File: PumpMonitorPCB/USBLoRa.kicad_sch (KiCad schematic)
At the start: 7 parts, among them J4 USB_C_Receptacle_USB2.0_16P, U7 WIO-SX1262, U8 TPD3E001DRLR

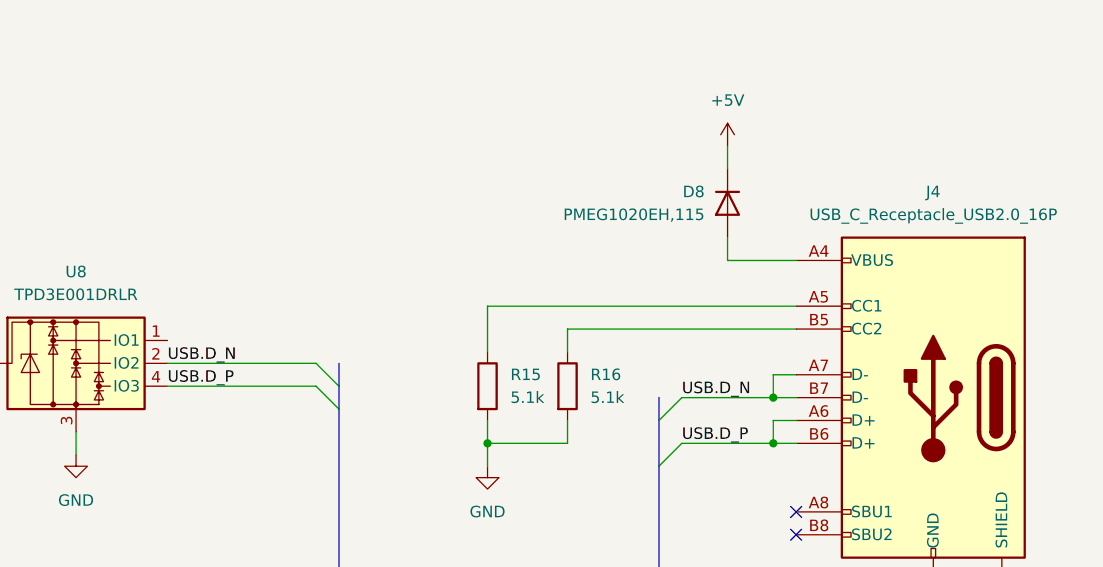
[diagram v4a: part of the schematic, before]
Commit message: Rejigged auxilliary connectors, experimetning with kiclearance.
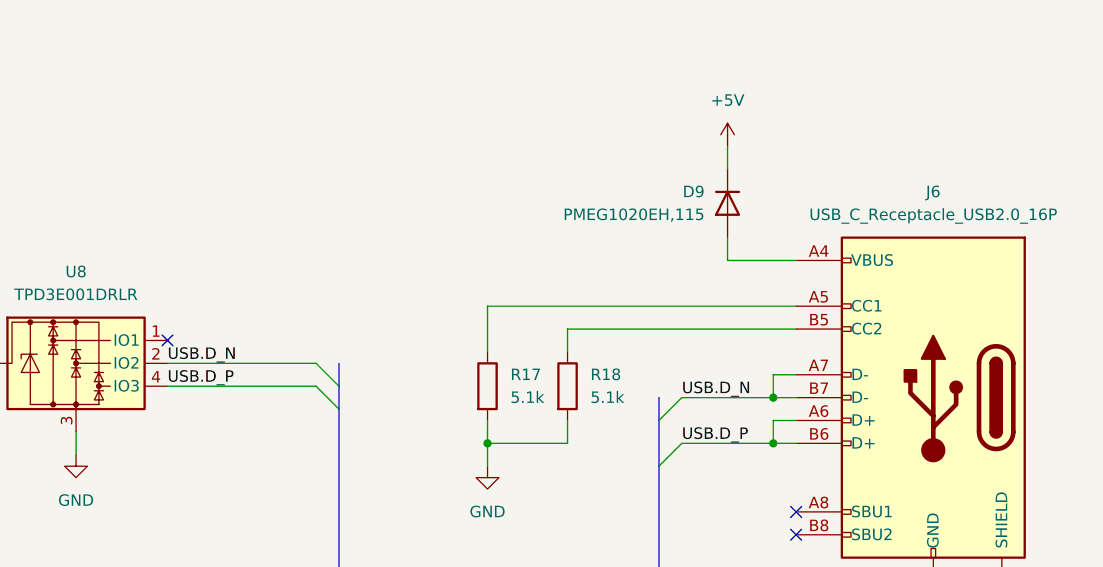
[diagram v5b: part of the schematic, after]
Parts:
- C17: footprint Capacitor_SMD:C_0805_2012Metric_Pad1.18x1.45mm_HandSolder -> Capacitor_SMD:C_0603_1608Metric_Pad1.08x0.95mm_HandSolder
- R17: renamed from R15; footprint Resistor_SMD:R_0805_2012Metric_Pad1.20x1.40mm_HandSolder -> Resistor_SMD:R_0603_1608Metric_Pad0.98x0.95mm_HandSolder; PlaceOnSecondary No -> (none)
- R18: renamed from R16; footprint Resistor_SMD:R_0805_2012Metric_Pad1.20x1.40mm_HandSolder -> Resistor_SMD:R_0603_1608Metric_Pad0.98x0.95mm_HandSolder; PlaceOnSecondary No -> (none)
- U8: PlaceOnSecondary No -> (none)
- renumbered D8 to D9, J4 to J6
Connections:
- no-connect marks 3 -> 4
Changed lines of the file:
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@@
 	(title_block
 		(title "Pump monitor - USB and LoRa transceiver")
-		(date "2025-09-25")
+		(date "2025-10-07")
 		(rev "V0.0.0")
 		(company "Jotham Gates")
+		(comment 1 "functionality depending on the application.")
+		(comment 2 "Components marked \"do not populate\" are optional and may be fitted to add additional")
 		(comment 4 "Warning: Parts of this circuit operate at mains potential.")
 	)
@@
 		(diameter 0)
 		(color 0 0 0 0)
+	)
+	(no_connect
+		(at 158.75 110.49)
 	)
 	(no_connect
@@
 		(dnp no)
 		(fields_autoplaced yes)
-		(property "Reference" "#PWR060"
+		(property "Reference" "#PWR062"
 			(at 148.59 129.54 0)
 			(effects
@@
 			(project "PumpMonitorPCB"
 				(path "/c90c4964-ca1b-44d9-8ea9-8989903af0f2/519408a1-89cc-4bd2-9b7b-cb03d2ff4d33/da0c16f9-ee3c-407f-b19e-ac24af140ef1"
-					(reference "#PWR060")
+					(reference "#PWR062")
 					(unit 1)
 				)
@@
 			)
 		)
-		(property "PlaceOnSecondary" "No"
-			(at 148.59 113.03 0)
-			(effects
-				(font
-					(size 1.27 1.27)
-				)
-				(hide yes)
-			)
-		)
 		(property "Sim.Device" ""
 			(at 148.59 113.03 0)
@@
 		)
 		(property "SchematicVersionModified" "V1.0.4"
+			(at 148.59 113.03 0)
+			(effects
+				(font
+					(size 1.27 1.27)
+				)
+				(hide yes)
+			)
+		)
+		(property "Part number" ""
 			(at 148.59 113.03 0)
 			(effects
@@
 			)
 		)
-		(property "Footprint" "Capacitor_SMD:C_0805_2012Metric_Pad1.18x1.45mm_HandSolder"
+		(property "Footprint" "Capacitor_SMD:C_0603_1608Metric_Pad1.08x0.95mm_HandSolder"
 			(at 144.4752 52.07 0)
 			(effects
@@
 		)
 		(property "Description" "Unpolarized capacitor"
+			(at 143.51 48.26 0)
+			(effects
+				(font
+					(size 1.27 1.27)
+				)
+				(hide yes)
+			)
+		)
+		(property "Part number" ""
 			(at 143.51 48.26 0)
 			(effects
@@
 		(dnp no)
 		(fields_autoplaced yes)
-		(property "Reference" "#PWR059"
+		(property "Reference" "#PWR061"
 			(at 143.51 60.96 0)
 			(effects
@@
 			(project "PumpMonitorPCB"
 				(path "/c90c4964-ca1b-44d9-8ea9-8989903af0f2/519408a1-89cc-4bd2-9b7b-cb03d2ff4d33/da0c16f9-ee3c-407f-b19e-ac24af140ef1"
-					(reference "#PWR059")
+					(reference "#PWR061")
 					(unit 1)
 				)
@@
 		(dnp no)
 		(fields_autoplaced yes)
-		(property "Reference" "#PWR056"
+		(property "Reference" "#PWR058"
 			(at 120.65 55.88 0)
 			(effects
@@
 			(project "PumpMonitorPCB"
 				(path "/c90c4964-ca1b-44d9-8ea9-8989903af0f2/519408a1-89cc-4bd2-9b7b-cb03d2ff4d33/da0c16f9-ee3c-407f-b19e-ac24af140ef1"
-					(reference "#PWR056")
+					(reference "#PWR058")
 					(unit 1)
 				)
@@
 		(dnp no)
 		(fields_autoplaced yes)
-		(property "Reference" "R16"
+		(property "Reference" "R18"
 			(at 205.74 114.2999 0)
 			(effects
@@
 			)
 		)
-		(property "Footprint" "Resistor_SMD:R_0805_2012Metric_Pad1.20x1.40mm_HandSolder"
+		(property "Footprint" "Resistor_SMD:R_0603_1608Metric_Pad0.98x0.95mm_HandSolder"
 			(at 201.422 115.57 90)
 			(effects
@@
 			)
 		)
-		(property "PlaceOnSecondary" "No"
-			(at 203.2 115.57 0)
-			(effects
-				(font
-					(size 1.27 1.27)
-				)
-				(hide yes)
-			)
-		)
 		(property "Sim.Device" ""
 			(at 203.2 115.57 0)
@@
 		)
 		(property "SchematicVersionModified" "V1.0.4"
+			(at 203.2 115.57 0)
+			(effects
+				(font
+					(size 1.27 1.27)
+				)
+				(hide yes)
+			)
+		)
+		(property "Part number" ""
 			(at 203.2 115.57 0)
 			(effects
@@
 			(project "PumpMonitorPCB"
 				(path "/c90c4964-ca1b-44d9-8ea9-8989903af0f2/519408a1-89cc-4bd2-9b7b-cb03d2ff4d33/da0c16f9-ee3c-407f-b19e-ac24af140ef1"
-					(reference "R16")
+					(reference "R18")
 					(unit 1)
 				)
@@
 		(dnp no)
 		(fields_autoplaced yes)
-		(property "Reference" "#PWR057"
+		(property "Reference" "#PWR059"
 			(at 135.89 114.3 0)
 			(effects
@@
 			(project "PumpMonitorPCB"
 				(path "/c90c4964-ca1b-44d9-8ea9-8989903af0f2/519408a1-89cc-4bd2-9b7b-cb03d2ff4d33/da0c16f9-ee3c-407f-b19e-ac24af140ef1"
-					(reference "#PWR057")
+					(reference "#PWR059")
 					(unit 1)
 				)
@@
 		(dnp no)
 		(fields_autoplaced yes)
-		(property "Reference" "R15"
+		(property "Reference" "R17"
 			(at 196.85 114.2999 0)
 			(effects
@@
 			)
 		)
-		(property "Footprint" "Resistor_SMD:R_0805_2012Metric_Pad1.20x1.40mm_HandSolder"
+		(property "Footprint" "Resistor_SMD:R_0603_1608Metric_Pad0.98x0.95mm_HandSolder"
 			(at 192.532 115.57 90)
 			(effects
@@
 			)
 		)
-		(property "PlaceOnSecondary" "No"
-			(at 194.31 115.57 0)
-			(effects
-				(font
-					(size 1.27 1.27)
-				)
-				(hide yes)
-			)
-		)
 		(property "Sim.Device" ""
 			(at 194.31 115.57 0)
@@
 		)
 		(property "SchematicVersionModified" "V1.0.4"
+			(at 194.31 115.57 0)
+			(effects
+				(font
+					(size 1.27 1.27)
+				)
+				(hide yes)
+			)
+		)
+		(property "Part number" ""
 			(at 194.31 115.57 0)
 			(effects
@@
 			(project "PumpMonitorPCB"
 				(path "/c90c4964-ca1b-44d9-8ea9-8989903af0f2/519408a1-89cc-4bd2-9b7b-cb03d2ff4d33/da0c16f9-ee3c-407f-b19e-ac24af140ef1"
-					(reference "R15")
+					(reference "R17")
 					(unit 1)
 				)
@@
 		(dnp no)
 		(fields_autoplaced yes)
-		(property "Reference" "#PWR054"
+		(property "Reference" "#PWR056"
 			(at 81.28 66.04 0)
 			(effects
@@
 			(project "PumpMonitorPCB"
 				(path "/c90c4964-ca1b-44d9-8ea9-8989903af0f2/519408a1-89cc-4bd2-9b7b-cb03d2ff4d33/da0c16f9-ee3c-407f-b19e-ac24af140ef1"
-					(reference "#PWR054")
+					(reference "#PWR056")
 					(unit 1)
 				)
@@
 		(on_board yes)
 		(dnp no)
-		(property "Reference" "J4"
+		(property "Reference" "J6"
 			(at 243.84 93.98 0)
 			(effects
@@
 		)
 		(property "Description" "USB 2.0-only 16P Type-C Receptacle connector"
+			(at 243.84 116.84 0)
+			(effects
+				(font
+					(size 1.27 1.27)
+				)
+				(hide yes)
+			)
+		)
+		(property "Part number" ""
 			(at 243.84 116.84 0)
 			(effects
@@
 			(project "PumpMonitorPCB"
 				(path "/c90c4964-ca1b-44d9-8ea9-8989903af0f2/519408a1-89cc-4bd2-9b7b-cb03d2ff4d33/da0c16f9-ee3c-407f-b19e-ac24af140ef1"
-					(reference "J4")
+					(reference "J6")
 					(unit 1)
 				)
@@
 			)
 		)
+		(property "Part number" ""
+			(at 105.41 46.99 0)
+			(effects
+				(font
+					(size 1.27 1.27)
+				)
+				(hide yes)
+			)
+		)
 		(pin "8"
 		)
@@
 		(dnp no)
 		(fields_autoplaced yes)
-		(property "Reference" "#PWR062"
+		(property "Reference" "#PWR064"
 			(at 220.98 92.71 0)
 			(effects
@@
 			(project "PumpMonitorPCB"
 				(path "/c90c4964-ca1b-44d9-8ea9-8989903af0f2/519408a1-89cc-4bd2-9b7b-cb03d2ff4d33/da0c16f9-ee3c-407f-b19e-ac24af140ef1"
-					(reference "#PWR062")
+					(reference "#PWR064")
 					(unit 1)
 				)
@@
 		(dnp no)
 		(fields_autoplaced yes)
-		(property "Reference" "#PWR055"
+		(property "Reference" "#PWR057"
 			(at 90.17 66.04 0)
 			(effects
@@
 			(project "PumpMonitorPCB"
 				(path "/c90c4964-ca1b-44d9-8ea9-8989903af0f2/519408a1-89cc-4bd2-9b7b-cb03d2ff4d33/da0c16f9-ee3c-407f-b19e-ac24af140ef1"
-					(reference "#PWR055")
+					(reference "#PWR057")
 					(unit 1)
 				)
@@
 		(dnp no)
 		(fields_autoplaced yes)
-		(property "Reference" "#PWR061"
+		(property "Reference" "#PWR063"
 			(at 194.31 130.81 0)
 			(effects
@@
 			(project "PumpMonitorPCB"
 				(path "/c90c4964-ca1b-44d9-8ea9-8989903af0f2/519408a1-89cc-4bd2-9b7b-cb03d2ff4d33/da0c16f9-ee3c-407f-b19e-ac24af140ef1"
-					(reference "#PWR061")
+					(reference "#PWR063")
 					(unit 1)
 				)
@@
 		(dnp no)
 		(fields_autoplaced yes)
-		(property "Reference" "#PWR058"
+		(property "Reference" "#PWR060"
 			(at 143.51 45.72 0)
 			(effects
@@
 			(project "PumpMonitorPCB"
 				(path "/c90c4964-ca1b-44d9-8ea9-8989903af0f2/519408a1-89cc-4bd2-9b7b-cb03d2ff4d33/da0c16f9-ee3c-407f-b19e-ac24af140ef1"
-					(reference "#PWR058")
+					(reference "#PWR060")
 					(unit 1)
 				)
@@
 		(dnp no)
 		(fields_autoplaced yes)
-		(property "Reference" "#PWR063"
+		(property "Reference" "#PWR065"
 			(at 243.84 151.13 0)
 			(effects
@@
 			(project "PumpMonitorPCB"
 				(path "/c90c4964-ca1b-44d9-8ea9-8989903af0f2/519408a1-89cc-4bd2-9b7b-cb03d2ff4d33/da0c16f9-ee3c-407f-b19e-ac24af140ef1"
-					(reference "#PWR063")
+					(reference "#PWR065")
 					(unit 1)
 				)
@@
 		(on_board yes)
 		(dnp no)
-		(property "Reference" "D8"
+		(property "Reference" "D9"
 			(at 218.44 93.9799 90)
 			(effects
@@
 		(property "Sim.Pins" "1=K 2=A"
 			(at 220.98 95.25 0)
+			(effects
+				(font
+					(size 1.27 1.27)
+				)
+				(hide yes)
+			)
+		)
+		(property "Part number" ""
+			(at 220.98 95.25 90)
 			(effects
 				(font
@@
 			(project "PumpMonitorPCB"
 				(path "/c90c4964-ca1b-44d9-8ea9-8989903af0f2/519408a1-89cc-4bd2-9b7b-cb03d2ff4d33/da0c16f9-ee3c-407f-b19e-ac24af140ef1"
-					(reference "D8")
+					(reference "D9")
 					(unit 1)
 				)

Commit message: Adding test points, CAD files
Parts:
- C17: DigikeyNumber (none) -> 311-1088-1-ND
- D9: DigikeyNumber (none) -> 1727-3849-1-ND
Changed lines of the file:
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@@
+			)
+		)
+		(property "DigikeyNumber" ""
+			(at 148.59 113.03 0)
+			(effects
+				(font
+					(size 1.27 1.27)
+				)
+				(hide yes)
 			)
 		)
@@
 			)
 		)
+		(property "DigikeyNumber" "311-1088-1-ND"
+			(at 143.51 48.26 0)
+			(effects
+				(font
+					(size 1.27 1.27)
+				)
+				(hide yes)
+			)
+		)
 		(pin "1"
 		)
@@
 			)
 		)
+		(property "DigikeyNumber" ""
+			(at 203.2 115.57 0)
+			(effects
+				(font
+					(size 1.27 1.27)
+				)
+				(hide yes)
+			)
+		)
 		(pin "2"
 		)
@@
 			)
 		)
+		(property "DigikeyNumber" ""
+			(at 194.31 115.57 0)
+			(effects
+				(font
+					(size 1.27 1.27)
+				)
+				(hide yes)
+			)
+		)
 		(pin "2"
 		)
@@
 			)
 		)
+		(property "DigikeyNumber" ""
+			(at 243.84 116.84 0)
+			(effects
+				(font
+					(size 1.27 1.27)
+				)
+				(hide yes)
+			)
+		)
 		(pin "A1"
 		)
@@
 			)
 		)
+		(property "DigikeyNumber" ""
+			(at 105.41 46.99 0)
+			(effects
+				(font
+					(size 1.27 1.27)
+				)
+				(hide yes)
+			)
+		)
 		(pin "8"
 		)
@@
 			(at 220.98 95.25 90)
 			(effects
+				(font
+					(size 1.27 1.27)
+				)
+				(hide yes)
+			)
+		)
+		(property "DigikeyNumber" "1727-3849-1-ND"
+			(at 220.98 95.25 90)
+			(effects
